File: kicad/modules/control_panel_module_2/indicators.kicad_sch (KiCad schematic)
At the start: 9 parts, among them U1 ULN2004A

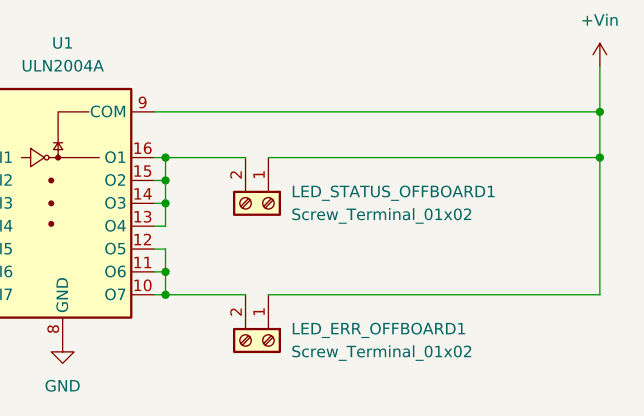
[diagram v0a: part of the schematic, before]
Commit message: Connector for bigger current, control module 2
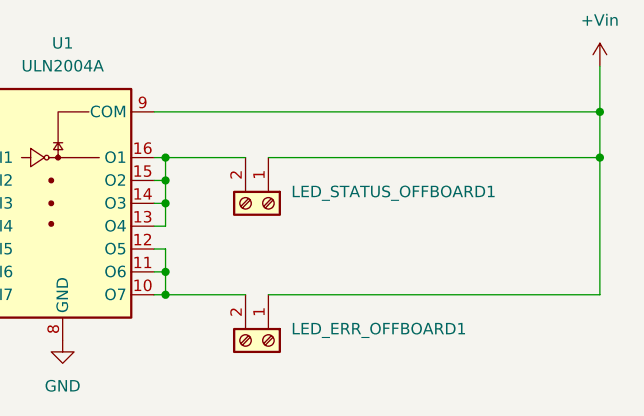
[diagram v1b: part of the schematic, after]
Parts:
- LED_ERR_OFFBOARD1, LED_STATUS_OFFBOARD1: value Screw_Terminal_01x02 -> ~
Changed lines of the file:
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@@
 			)
 		)
-		(property "Value" "Screw_Terminal_01x02"
+		(property "Value" "~"
 			(at 143.51 93.9799 90)
 			(effects
@@
 			)
 		)
-		(property "Value" "Screw_Terminal_01x02"
+		(property "Value" "~"
 			(at 143.51 78.7399 90)
 			(effects

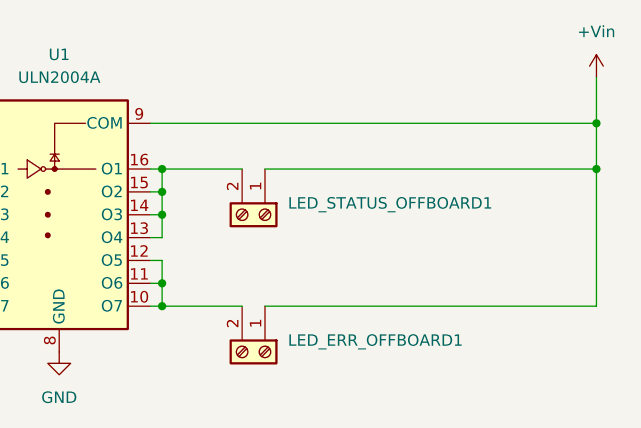
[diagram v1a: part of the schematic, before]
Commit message: Add part numbers
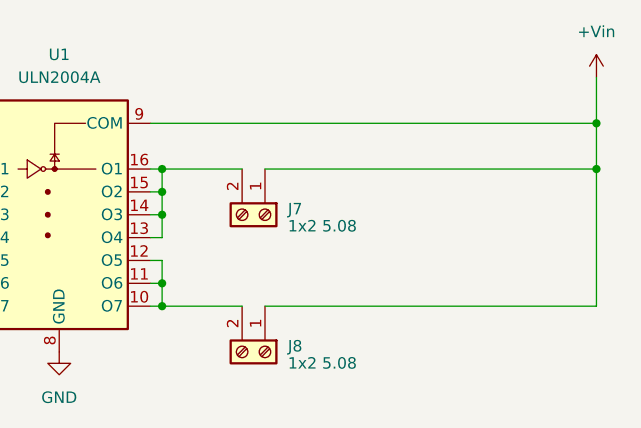
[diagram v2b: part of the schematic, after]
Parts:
- D1: Manufacturer Part Number (none) -> VLMG1300-GS08
- D2: Manufacturer Part Number (none) -> VLMO1300-GS08
- D3: Manufacturer Part Number (none) -> VLMS1300-GS08
- J7: renamed from LED_STATUS_OFFBOARD1; value ~ -> 1x2 5.08; Manufacturer Part Number (none) -> TB0012-508-02GR; Mouser number (none) -> 179-TB0012-508-02GR
- J8: renamed from LED_ERR_OFFBOARD1; value ~ -> 1x2 5.08; Manufacturer Part Number (none) -> TB0012-508-02GR; Mouser number (none) -> 179-TB0012-508-02GR
- R4, R5, R6: Manufacturer Part Number (none) -> CRCW06031K00FKEA
- U1: Manufacturer Part Number (none) -> ULN2004ADR
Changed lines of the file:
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@@
 		(dnp no)
 		(fields_autoplaced yes)
-		(property "Reference" "LED_ERR_OFFBOARD1"
-			(at 143.51 91.4399 90)
+		(property "Reference" "J8"
+			(at 143.51 92.0749 90)
 			(effects
 				(font
@@
 			)
 		)
-		(property "Value" "~"
-			(at 143.51 93.9799 90)
+		(property "Value" "1x2 5.08"
+			(at 143.51 93.98 90)
 			(effects
 				(font
@@
 			)
 		)
-		(property "Description" "Generic screw terminal, single row, 01x02, script generated (kicad-library-utils/schlib/autogen/connector/)"
+		(property "Description" "CUSTOM"
 			(at 140.97 92.71 0)
 			(effects
@@
 			)
 		)
-		(property "Manufacturer Part Number" ""
+		(property "Manufacturer Part Number" "TB0012-508-02GR"
 			(at 140.97 92.71 0)
 			(effects
@@
 			)
 		)
-		(property "Mouser number" ""
+		(property "Mouser number" "179-TB0012-508-02GR"
 			(at 140.97 92.71 0)
 			(effects
@@
 			(project "control_panel_module"
 				(path "/01f48663-51d7-48f4-9aa9-9279c565a6cb/da3882a4-de83-4b7b-a911-0ab86609a0d0"
-					(reference "LED_ERR_OFFBOARD1")
+					(reference "J8")
 					(unit 1)
 				)
@@
 			)
 		)
-		(property "Description" ""
+		(property "Description" "ULM"
 			(at 33.02 36.83 0)
 			(effects
@@
 			)
 		)
-		(property "Manufacturer Part Number" ""
+		(property "Manufacturer Part Number" "CRCW06031K00FKEA"
 			(at 33.02 36.83 0)
 			(effects
@@
 			)
 		)
-		(property "Description" ""
+		(property "Description" "ULM"
 			(at 48.26 44.45 0)
 			(effects
@@
 			)
 		)
-		(property "Manufacturer Part Number" ""
+		(property "Manufacturer Part Number" "VLMO1300-GS08"
 			(at 48.26 44.45 0)
 			(effects
@@
 			)
 		)
-		(property "Description" ""
+		(property "Description" "ULM"
 			(at 64.77 44.45 0)
 			(effects
@@
 			)
 		)
-		(property "Manufacturer Part Number" ""
+		(property "Manufacturer Part Number" "VLMS1300-GS08"
 			(at 64.77 44.45 0)
 			(effects
@@
 			)
 		)
-		(property "Description" ""
+		(property "Description" "ULM"
 			(at 64.77 36.83 0)
 			(effects
@@
 			)
 		)
-		(property "Manufacturer Part Number" ""
+		(property "Manufacturer Part Number" "CRCW06031K00FKEA"
 			(at 64.77 36.83 0)
 			(effects
@@
 			)
 		)
-		(property "Description" ""
+		(property "Description" "ULM"
 			(at 48.26 36.83 0)
 			(effects
@@
 			)
 		)
-		(property "Manufacturer Part Number" ""
+		(property "Manufacturer Part Number" "CRCW06031K00FKEA"
 			(at 48.26 36.83 0)
 			(effects
@@
 		(dnp no)
 		(fields_autoplaced yes)
-		(property "Reference" "LED_STATUS_OFFBOARD1"
-			(at 143.51 76.1999 90)
+		(property "Reference" "J7"
+			(at 143.51 76.8349 90)
 			(effects
 				(font
@@
 			)
 		)
-		(property "Value" "~"
-			(at 143.51 78.7399 90)
+		(property "Value" "1x2 5.08"
+			(at 143.51 78.74 90)
 			(effects
 				(font
@@
 			)
 		)
-		(property "Description" "Generic screw terminal, single row, 01x02, script generated (kicad-library-utils/schlib/autogen/connector/)"
+		(property "Description" "CUSTOM"
 			(at 140.97 77.47 0)
 			(effects
@@
 			)
 		)
-		(property "Manufacturer Part Number" ""
+		(property "Manufacturer Part Number" "TB0012-508-02GR"
 			(at 140.97 77.47 0)
 			(effects
@@
 			)
 		)
-		(property "Mouser number" ""
+		(property "Mouser number" "179-TB0012-508-02GR"
 			(at 140.97 77.47 0)
 			(effects
@@
 			(project "control_panel_module"
 				(path "/01f48663-51d7-48f4-9aa9-9279c565a6cb/da3882a4-de83-4b7b-a911-0ab86609a0d0"
-					(reference "LED_STATUS_OFFBOARD1")
+					(reference "J7")
 					(unit 1)
 				)
@@
 			)
 		)
-		(property "Description" ""
+		(property "Description" "CUSTOM"
 			(at 118.11 77.47 0)
 			(effects
@@
 			)
 		)
-		(property "Manufacturer Part Number" ""
+		(property "Manufacturer Part Number" "ULN2004ADR"
 			(at 118.11 77.47 0)
 			(effects
@@
 			)
 		)
-		(property "Description" ""
+		(property "Description" "ULM"
 			(at 33.02 44.45 0)
 			(effects
@@
 			)
 		)
-		(property "Manufacturer Part Number" ""
+		(property "Manufacturer Part Number" "VLMG1300-GS08 "
 			(at 33.02 44.45 0)
 			(effects

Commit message: BOM with Ullmanna part numbers
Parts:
- D1: Manufacturer Part Number VLMG1300-GS08 -> APTD1608LCGCK; Mouser number 78-VLMG1300-GS08 -> 604-APTD1608LCGCK; Ullmanna Part Number (none) -> BMCLED002
- D2: Manufacturer Part Number VLMO1300-GS08 -> APTD1608LSYCK; Mouser number 78-VLMO1300-GS08 -> 604-APTD1608LSYCK; Ullmanna Part Number (none) -> BMCLED003
- D3: Manufacturer Part Number VLMS1300-GS08 -> APTD1608LSURCK; Mouser number 78-VLMS1300-GS08 -> 604-APTD1608LSURCK; Ullmanna Part Number (none) -> BMCLED004
- R4, R5, R6: Manufacturer Part Number CRCW06031K00FKEA -> RC0603FR-071KL; Mouser number 71-CRCW0603-1.0K-E3 -> 603-RC0603FR-071KL; Ullmanna Part Number (none) -> BMCR0176
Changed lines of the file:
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@@
 (kicad_sch
-	(version 20231120)
+	(version 20250114)
 	(generator "eeschema")
-	(generator_version "8.0")
+	(generator_version "9.0")
 	(paper "A5")
 	(junction
@@
 		(shape input)
 		(at 64.77 30.48 90)
-		(fields_autoplaced yes)
 		(effects
 			(font
@@
 		(shape input)
 		(at 101.6 87.63 180)
-		(fields_autoplaced yes)
 		(effects
 			(font
@@
 		(shape input)
 		(at 101.6 72.39 180)
-		(fields_autoplaced yes)
 		(effects
 			(font
@@
 		(shape input)
 		(at 48.26 30.48 90)
-		(fields_autoplaced yes)
 		(effects
 			(font
@@
 			)
 		)
+		(property "Ullmanna Part Number" ""
+			(at 140.97 92.71 90)
+			(effects
+				(font
+					(size 1.27 1.27)
+				)
+				(hide yes)
+			)
+		)
 		(pin "2"
 		)
@@
 			)
 		)
-		(property "Manufacturer Part Number" "CRCW06031K00FKEA"
+		(property "Manufacturer Part Number" "RC0603FR-071KL"
 			(at 33.02 36.83 0)
 			(effects
@@
 			)
 		)
-		(property "Mouser number" "71-CRCW0603-1.0K-E3"
+		(property "Mouser number" "603-RC0603FR-071KL"
+			(at 33.02 36.83 0)
+			(effects
+				(font
+					(size 1.27 1.27)
+				)
+				(hide yes)
+			)
+		)
+		(property "Ullmanna Part Number" "BMCR0176"
 			(at 33.02 36.83 0)
 			(effects
@@
 			)
 		)
-		(property "Manufacturer Part Number" "VLMO1300-GS08"
+		(property "Manufacturer Part Number" "APTD1608LSYCK"
 			(at 48.26 44.45 0)
 			(effects
@@
 			)
 		)
-		(property "Mouser number" "78-VLMO1300-GS08"
+		(property "Mouser number" "604-APTD1608LSYCK"
+			(at 48.26 44.45 0)
+			(effects
+				(font
+					(size 1.27 1.27)
+				)
+				(hide yes)
+			)
+		)
+		(property "Ullmanna Part Number" "BMCLED003"
 			(at 48.26 44.45 0)
 			(effects
@@
 			)
 		)
-		(property "Manufacturer Part Number" "VLMS1300-GS08"
+		(property "Manufacturer Part Number" "APTD1608LSURCK"
 			(at 64.77 44.45 0)
 			(effects
@@
 			)
 		)
-		(property "Mouser number" "78-VLMS1300-GS08"
+		(property "Mouser number" "604-APTD1608LSURCK"
+			(at 64.77 44.45 0)
+			(effects
+				(font
+					(size 1.27 1.27)
+				)
+				(hide yes)
+			)
+		)
+		(property "Ullmanna Part Number" "BMCLED004"
 			(at 64.77 44.45 0)
 			(effects
@@
 			)
 		)
-		(property "Manufacturer Part Number" "CRCW06031K00FKEA"
+		(property "Manufacturer Part Number" "RC0603FR-071KL"
 			(at 64.77 36.83 0)
 			(effects
@@
 			)
 		)
-		(property "Mouser number" "71-CRCW0603-1.0K-E3"
+		(property "Mouser number" "603-RC0603FR-071KL"
+			(at 64.77 36.83 0)
+			(effects
+				(font
+					(size 1.27 1.27)
+				)
+				(hide yes)
+			)
+		)
+		(property "Ullmanna Part Number" "BMCR0176"
 			(at 64.77 36.83 0)
 			(effects
@@
 			)
 		)
-		(property "Manufacturer Part Number" "CRCW06031K00FKEA"
+		(property "Manufacturer Part Number" "RC0603FR-071KL"
 			(at 48.26 36.83 0)
 			(effects
@@
 			)
 		)
-		(property "Mouser number" "71-CRCW0603-1.0K-E3"
+		(property "Mouser number" "603-RC0603FR-071KL"
+			(at 48.26 36.83 0)
+			(effects
+				(font
+					(size 1.27 1.27)
+				)
+				(hide yes)
+			)
+		)
+		(property "Ullmanna Part Number" "BMCR0176"
 			(at 48.26 36.83 0)
 			(effects
@@
 			)
 		)
+		(property "Ullmanna Part Number" ""
+			(at 140.97 77.47 90)
+			(effects
+				(font
+					(size 1.27 1.27)
+				)
+				(hide yes)
+			)
+		)
 		(pin "2"
 		)
@@
 			)
 		)
+		(property "Ullmanna Part Number" ""
+			(at 118.11 77.47 0)
+			(effects
+				(font
+					(size 1.27 1.27)
+				)
+				(hide yes)
+			)
+		)
 		(pin "8"
 		)
@@
 			)
 		)
-		(property "Manufacturer Part Number" "VLMG1300-GS08 "
+		(property "Manufacturer Part Number" "APTD1608LCGCK"
 			(at 33.02 44.45 0)
 			(effects
@@
 			)
 		)
-		(property "Mouser number" "78-VLMG1300-GS08"
+		(property "Mouser number" "604-APTD1608LCGCK"
 			(at 33.02 44.45 0)
 			(effects
+				(font
+					(size 1.27 1.27)
+				)
+				(hide yes)
+			)
+		)
+		(property "Ullmanna Part Number" "BMCLED002"
+			(at 33.02 44.45 0)
+			(effects

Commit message: LED footprint update
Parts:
- D1: footprint LED_SMD:LED_0603_1608Metric_Pad1.05x0.95mm_HandSolder -> LED_SMD:LED_0805_2012Metric_Pad1.15x1.40mm_HandSolder; Manufacturer Part Number APTD1608LCGCK -> APTD2012LCGCK; Mouser number 604-APTD1608LCGCK -> 604-APTD2012LCGCK; Ullmanna Part Number BMCLED002 -> BMCLED102
- D2: footprint LED_SMD:LED_0603_1608Metric_Pad1.05x0.95mm_HandSolder -> LED_SMD:LED_0805_2012Metric_Pad1.15x1.40mm_HandSolder; Manufacturer Part Number APTD1608LSYCK -> APTD2012LSYCK; Mouser number 604-APTD1608LSYCK -> 604-APTD2012LSYCK; Ullmanna Part Number BMCLED003 -> BMCLED103
- D3: footprint LED_SMD:LED_0603_1608Metric_Pad1.05x0.95mm_HandSolder -> LED_SMD:LED_0805_2012Metric_Pad1.15x1.40mm_HandSolder; Manufacturer Part Number APTD1608LSURCK -> APTD2012LSURCK; Mouser number 604-APTD1608LSURCK -> 604-APTD2012LSURCK; Ullmanna Part Number BMCLED004 -> BMCLED104
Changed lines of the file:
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@@
 			)
 		)
-		(property "Footprint" "LED_SMD:LED_0603_1608Metric_Pad1.05x0.95mm_HandSolder"
+		(property "Footprint" "LED_SMD:LED_0805_2012Metric_Pad1.15x1.40mm_HandSolder"
 			(at 48.26 44.45 0)
 			(effects
@@
 			)
 		)
-		(property "Manufacturer Part Number" "APTD1608LSYCK"
+		(property "Manufacturer Part Number" "APTD2012LSYCK "
 			(at 48.26 44.45 0)
 			(effects
@@
 			)
 		)
-		(property "Mouser number" "604-APTD1608LSYCK"
+		(property "Mouser number" "604-APTD2012LSYCK "
 			(at 48.26 44.45 0)
 			(effects
@@
 			)
 		)
-		(property "Ullmanna Part Number" "BMCLED003"
+		(property "Ullmanna Part Number" "BMCLED103 "
 			(at 48.26 44.45 0)
 			(effects
@@
 			)
 		)
-		(property "Footprint" "LED_SMD:LED_0603_1608Metric_Pad1.05x0.95mm_HandSolder"
+		(property "Footprint" "LED_SMD:LED_0805_2012Metric_Pad1.15x1.40mm_HandSolder"
 			(at 64.77 44.45 0)
 			(effects
@@
 			)
 		)
-		(property "Manufacturer Part Number" "APTD1608LSURCK"
+		(property "Manufacturer Part Number" "APTD2012LSURCK "
 			(at 64.77 44.45 0)
 			(effects
@@
 			)
 		)
-		(property "Mouser number" "604-APTD1608LSURCK"
+		(property "Mouser number" "604-APTD2012LSURCK "
 			(at 64.77 44.45 0)
 			(effects
@@
 			)
 		)
-		(property "Ullmanna Part Number" "BMCLED004"
+		(property "Ullmanna Part Number" "BMCLED104 "
 			(at 64.77 44.45 0)
 			(effects
@@
 			)
 		)
-		(property "Footprint" "LED_SMD:LED_0603_1608Metric_Pad1.05x0.95mm_HandSolder"
+		(property "Footprint" "LED_SMD:LED_0805_2012Metric_Pad1.15x1.40mm_HandSolder"
 			(at 33.02 44.45 0)
 			(effects
@@
 			)
 		)
-		(property "Manufacturer Part Number" "APTD1608LCGCK"
+		(property "Manufacturer Part Number" "APTD2012LCGCK "
 			(at 33.02 44.45 0)
 			(effects
@@
 			)
 		)
-		(property "Mouser number" "604-APTD1608LCGCK"
+		(property "Mouser number" "604-APTD2012LCGCK "
 			(at 33.02 44.45 0)
 			(effects
@@
 			)
 		)
-		(property "Ullmanna Part Number" "BMCLED002"
+		(property "Ullmanna Part Number" "BMCLED102 "
 			(at 33.02 44.45 0)
 			(effects
